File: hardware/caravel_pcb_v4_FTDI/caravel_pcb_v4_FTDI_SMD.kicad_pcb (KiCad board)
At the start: 2 copper layers, 76.2 x 73.8 mm, 65 parts, among them J1 USB_B_Micro - 10118193-0001LF, J10 Conn_01x27_Female, J11 Conn_01x20_Female, J2 Conn_01x02_Female, J3 Conn_01x02_Male, J4 Conn_01x04_Female, J5 Conn_01x02_Male, J6 Conn_01x02_Male, J7 Conn_01x06_Female, J8 Conn_01x02_Male, J9 Conn_01x02_Male, SW1 SW_Push - SKQGADE010, T1 Logo, T2 Logo, U1 FT232H, U2 SN74LVC1G125DCKR, U3 SN74LVC1G125DCKR, U4 AZ1117CH-1.8TRG1, U5 AZ1117-3.3, U6 caravel_breakout, U7 W25Q32FVSS, X1 DSC6001_10MHZ, Y1 CSTNE12M0GH5L000R0

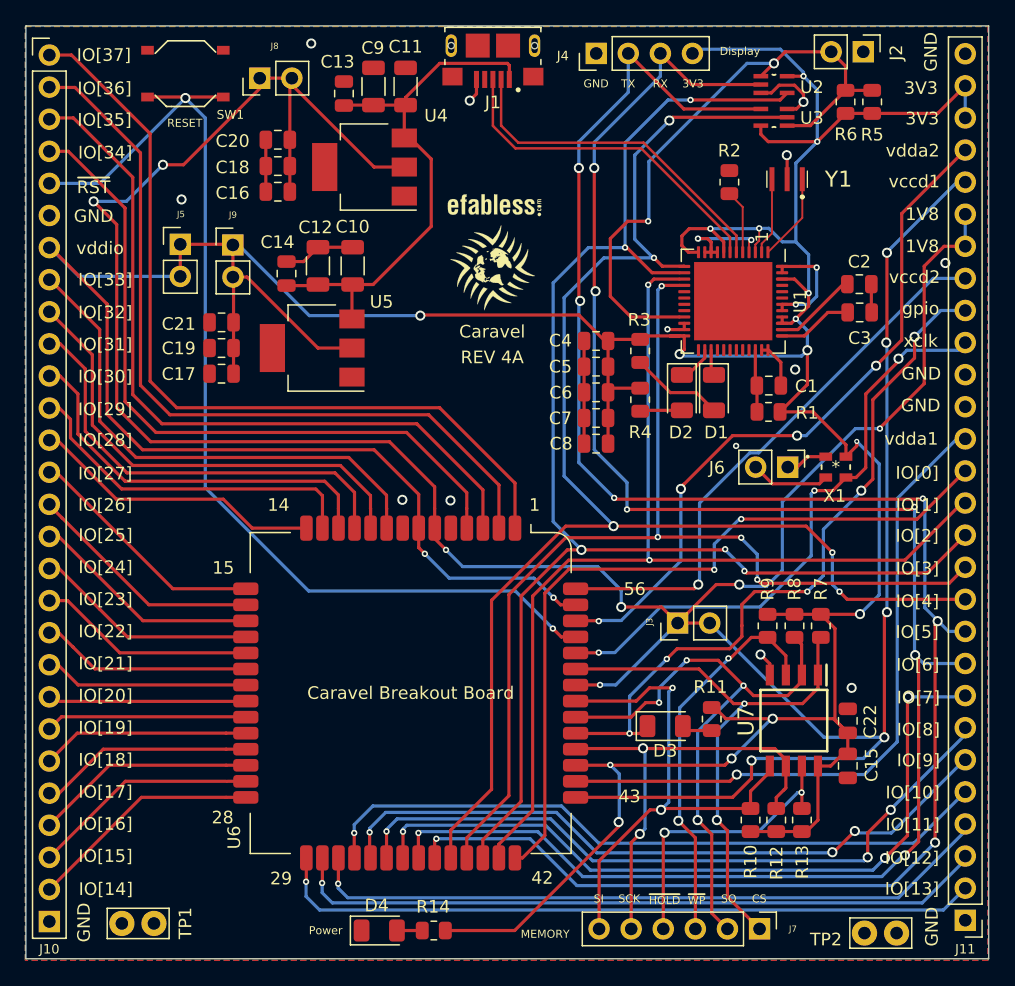
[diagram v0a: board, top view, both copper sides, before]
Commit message: update caravel FTDI mainboard V4 (Rev 4B)
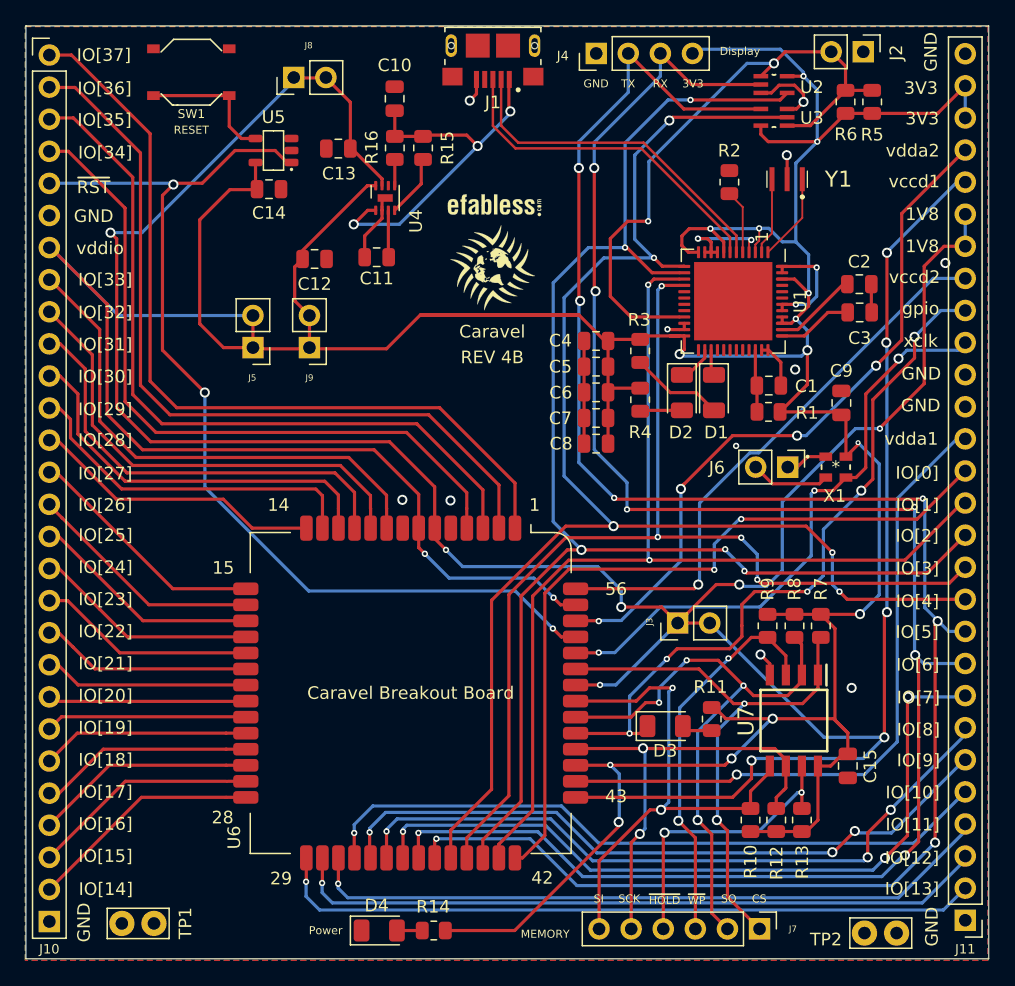
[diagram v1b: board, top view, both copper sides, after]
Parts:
- removed C16, C17: 22uf - CC0805MKX5R5BB226, Capacitor_SMD:C_0805_2012Metric
- removed C18, C19: 10uf - CC0805KKX5R8BB106, Capacitor_SMD:C_0805_2012Metric
- removed C20, C21: 1uf, Capacitor_SMD:C_0805_2012Metric
- removed C22: 0.1uf - CC0805KRX7R9BB104, Capacitor_SMD:C_0805_2012Metric
- added R15: 10k, Resistor_SMD:R_0805_2012Metric, F.Cu at (131.4, 68.4)
- added R16: 10k, Resistor_SMD:R_0805_2012Metric, F.Cu at (129.2, 68.4)
- C10: value 100uf - GRM31CR60J107ME39L -> 10uf - CC0805KKX5R8BB106; footprint Capacitor_SMD:C_1206_3216Metric -> Capacitor_SMD:C_0805_2012Metric
- C11, C9: value 100uf - GRM31CR60J107ME39L -> 0.1uf - CC0805KRX7R9BB104; footprint Capacitor_SMD:C_1206_3216Metric -> Capacitor_SMD:C_0805_2012Metric
- C12: value 100uf - GRM31CR60J107ME39L -> 2.2uf - CC0805MKX5R6BB225; footprint Capacitor_SMD:C_1206_3216Metric -> Capacitor_SMD:C_0805_2012Metric
- C13: value 10uf - CC0805KKX5R8BB106 -> 2.2uf - CC0805MKX5R6BB225
- C14: value 10uf - CC0805KKX5R8BB106 -> 0.1uf - CC0805KRX7R9BB104
- U4: value AZ1117CH-1.8TRG1 -> MIC5350-SGYMT-TR; footprint Package_TO_SOT_SMD:SOT-223 -> Package_DFN_QFN:DFN-8-1EP_2x2mm_P0.5mm_EP0.6x1.2mm
- U5: value AZ1117-3.3 -> MCP1319MT-29LE-OT; footprint Package_TO_SOT_SMD:SOT-223 -> Caravel_Board:PoR_5_SOT23
- moved C9 44.7 mm to (164.5, 88.6)
- moved U5 15.9 mm to (119.6, 68.6)
- moved C11 13.7 mm to (127.8, 77.1), turned to 180 degrees
- moved C10 13.6 mm to (129.2, 64.5)
- moved J9 10.1 mm to (122.4, 84.2), turned to 180 degrees
- moved J5 10.00 mm to (118.0, 84.2), turned to 180 degrees
- moved C14 6.82 mm to (119.2, 71.7), turned to 180 degrees
- moved C13 4.38 mm to (124.7, 68.5), turned to 0 degrees
- moved U4 2.95 mm to (128.4, 72.4), turned to 90 degrees
- moved J8 2.69 mm to (121.2, 62.8)
- moved C12 0.61 mm to (122.8, 77.2), turned to 180 degrees
- moved SW1 0.48 mm to (113.1, 62.4)
- turned C15 to -90 degrees
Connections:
- C11 pad 1: GND -> Net-(C11-Pad1)
- C11 pad 2: +5V -> GND
- C12 pad 2: +5V -> vdda
- C13 pad 2: +5V -> vccd
- C14 pad 2: +5V -> vdda
- C15 pad 1: GND -> vdda
- C15 pad 2: vdda -> GND
- C9 pad 2: +5V -> vdda
- SW1 pad 1: ~{RST} -> ~{MR}
- U4 pad 1: GND -> +5V
- U4 pad 2: vccd -> GND
- U4 pad 3: +5V -> Net-(C11-Pad1)
- U4 pad 4: (no net) -> Net-(R15-Pad1)
- U5 pad 1: GND -> ~{RST}
- U5 pad 2: vdda -> GND
- U5 pad 3: +5V -> unconnected-(U5-Pad3)
- U5 pad 4: (no net) -> ~{MR}
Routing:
- net vdda: track 353.6 -> 382.0 mm, vias 17 -> 16
- net +5V: track 43.1 -> 29.1 mm, vias 0 -> 3
- net vccd: track 264.4 -> 252.4 mm, vias 12 -> 11
- net ~{MR}: track 0.00 -> 10.8 mm
- net ~{RST}: track 85.3 -> 80.4 mm, vias 2 -> 3
- net GND: track 61.2 -> 56.3 mm, vias 17 -> 15
- net Net-(R15-Pad1): track 0.00 -> 4.75 mm
- net Net-(C11-Pad1): track 0.00 -> 3.80 mm
- net Net-(R16-Pad1): track 0.00 -> 2.16 mm
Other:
- board text added: "REV 4B"
- board text removed: "REV 4A"

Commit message: update caravel FTDI mainboard V4 (Rev 4B) to support different LDO devices with the same footprint
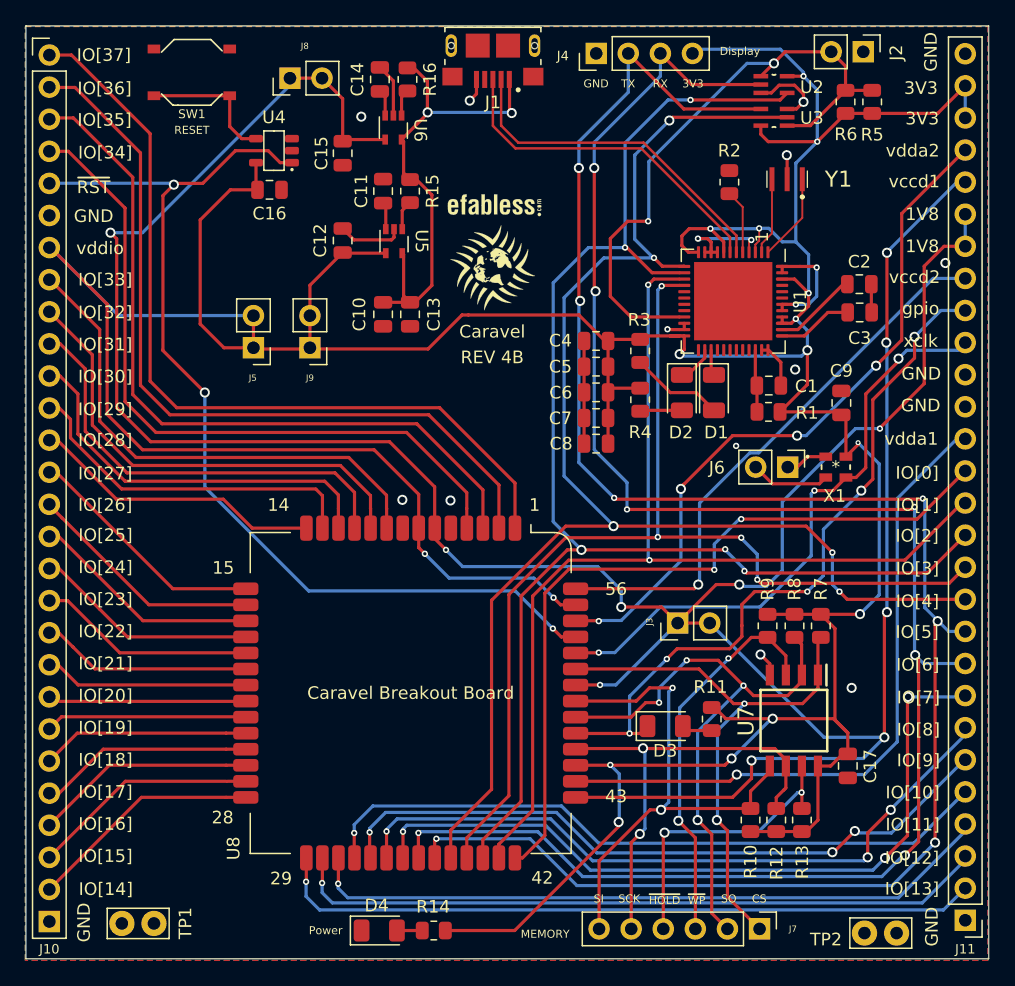
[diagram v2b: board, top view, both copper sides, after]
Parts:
- added C15: 10uf - CC0805KKX5R8BB106, Capacitor_SMD:C_0805_2012Metric, F.Cu at (125.1, 68.8)
- added C16: 0.1uf - CC0805KRX7R9BB104, Capacitor_SMD:C_0805_2012Metric, F.Cu at (119.3, 71.7)
- added U6: TAR5SxxU_SOT353F, Caravel_Board:SOT-353F, F.Cu at (129.1, 66.8)
- C10: value 10uf - CC0805KKX5R8BB106 -> 1uf - CC0805KKX5R8BB105
- C11, C14: value 0.1uf - CC0805KRX7R9BB104 -> 0.01uf - CC0805KRX7R9BB103
- C12: value 2.2uf - CC0805MKX5R6BB225 -> 10uf - CC0805KKX5R8BB106
- C13: value 2.2uf - CC0805MKX5R6BB225 -> 1uf - CC0805KKX5R8BB105
- U4: value MIC5350-SGYMT-TR -> MCP1319MT-29LE-OT; footprint Package_DFN_QFN:DFN-8-1EP_2x2mm_P0.5mm_EP0.6x1.2mm -> Caravel_Board:PoR_5_SOT23
- U5: value MCP1319MT-29LE-OT -> TAR5SxxU_SOT353F; footprint Caravel_Board:PoR_5_SOT23 -> Caravel_Board:SOT-353F
- moved C10 17.1 mm to (128.3, 81.6), turned to 90 degrees
- moved C13 14.3 mm to (130.4, 81.6), turned to 90 degrees
- moved C14 12.3 mm to (128.0, 63.0), turned to 90 degrees
- moved U5 11.9 mm to (129.1, 75.8), turned to -90 degrees
- moved U4 9.57 mm to (119.6, 68.6), turned to 180 degrees
- moved R16 5.51 mm to (130.2, 63.0)
- moved C11 5.26 mm to (128.3, 71.8), turned to 90 degrees
- moved R15 3.57 mm to (130.4, 71.8)
- moved C12 2.66 mm to (125.1, 75.7), turned to -90 degrees
- moved J8 0.31 mm to (120.9, 62.9)
- renumbered C15 to C17, U6 to U8
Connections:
- C11 pad 1: Net-(C11-Pad1) -> Net-(U5-Pad3)
- C13 pad 2: vccd -> +5V
- C14 pad 1: GND -> Net-(C14-Pad1)
- C14 pad 2: vdda -> GND
- R15 pad 1: Net-(R15-Pad1) -> Net-(U5-Pad1)
- U4 pad 1: +5V -> ~{RST}
- U4 pad 3: Net-(C11-Pad1) -> unconnected-(U4-Pad3)
- U4 pad 4: Net-(R15-Pad1) -> ~{MR}
- U4 pad 5: Net-(R16-Pad1) -> vdda
- U5 pad 1: ~{RST} -> Net-(U5-Pad1)
- U5 pad 3: unconnected-(U5-Pad3) -> Net-(U5-Pad3)
- U5 pad 4: ~{MR} -> vdda
- U5 pad 5: vdda -> +5V
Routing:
- net vdda: track 382.0 -> 366.3 mm
- net +5V: track 29.1 -> 38.1 mm, vias 3 -> 2
- net Net-(R15-Pad1): track 4.75 -> 0.00 mm
- net GND: track 56.3 -> 60.7 mm, vias 15 -> 16
- net Net-(C11-Pad1): track 3.80 -> 0.00 mm
- net Net-(U5-Pad1): track 0.00 -> 2.36 mm
- net Net-(U5-Pad3): track 0.00 -> 2.15 mm
- net Net-(C14-Pad1): track 0.00 -> 2.08 mm
- net vccd: track 252.4 -> 251.3 mm
